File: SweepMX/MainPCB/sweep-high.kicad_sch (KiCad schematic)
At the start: 54 parts, among them J1 AudioJack4dpb, J2 AudioJack4dpb, SW10 SW_Push, SW10_r1 SW_Push, SW11 SW_Push, SW11_r1 SW_Push, SW12 SW_Push, SW12_r1 SW_Push, SW13_r1 SW_Push, SW14 SW_Push, SW14_r1 SW_Push, SW15 SW_Push, SW15_r1 SW_Push, SW16 SW_Push, SW16_r1 SW_Push, SW17 SW_Push, SW17_r1 SW_Push, SW18 SW_Push, SW18_r1 SW_Push, SW2 SW_Push, SW20 SW_Push, SW21 SW_Push, SW2_r1 SW_Push, SW3 SW_Push, SW3_r1 SW_Push, SW4 SW_Push, SW4_r1 SW_Push, SW5 SW_Push, SW5_r1 SW_Push, SW6 SW_Push, SW6_r1 SW_Push, SW7_r1 SW_Push, SW8 SW_Push, SW8_r1 SW_Push, SW9 SW_Push, SW9_r1 SW_Push, U1 ProMicro-kbd, U2 ProMicro-kbd

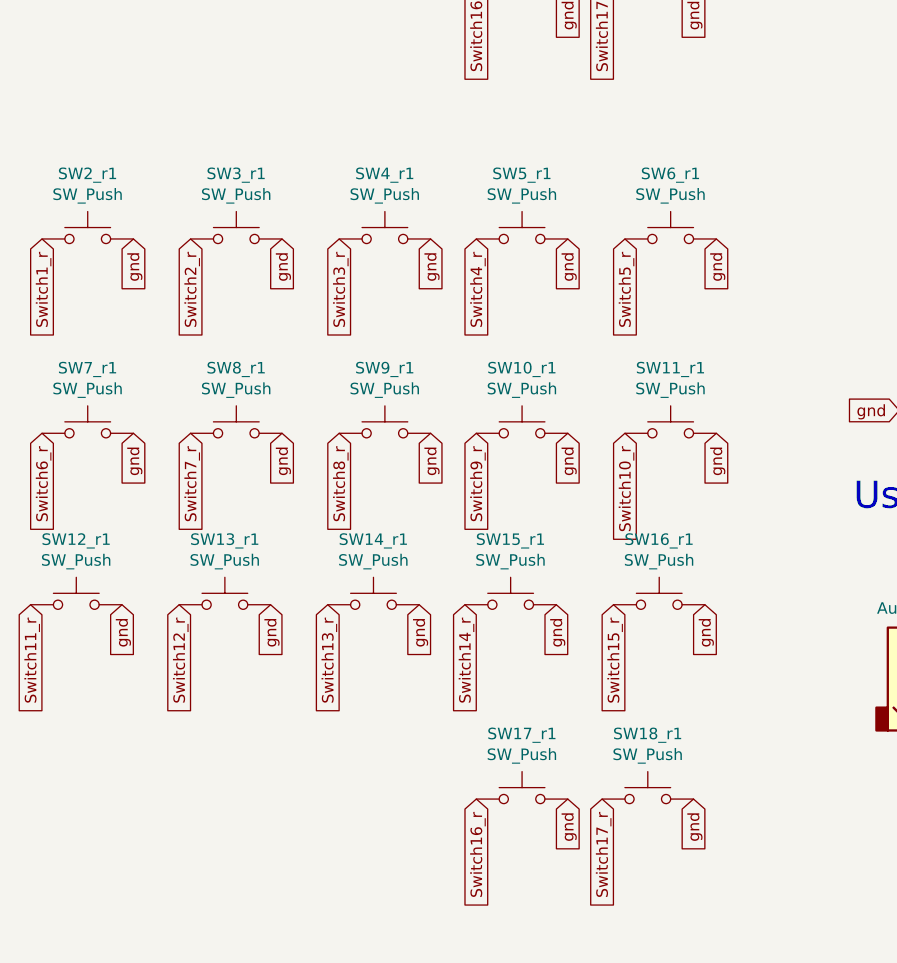
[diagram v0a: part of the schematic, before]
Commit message: sorted schematic and PCB for MX ver
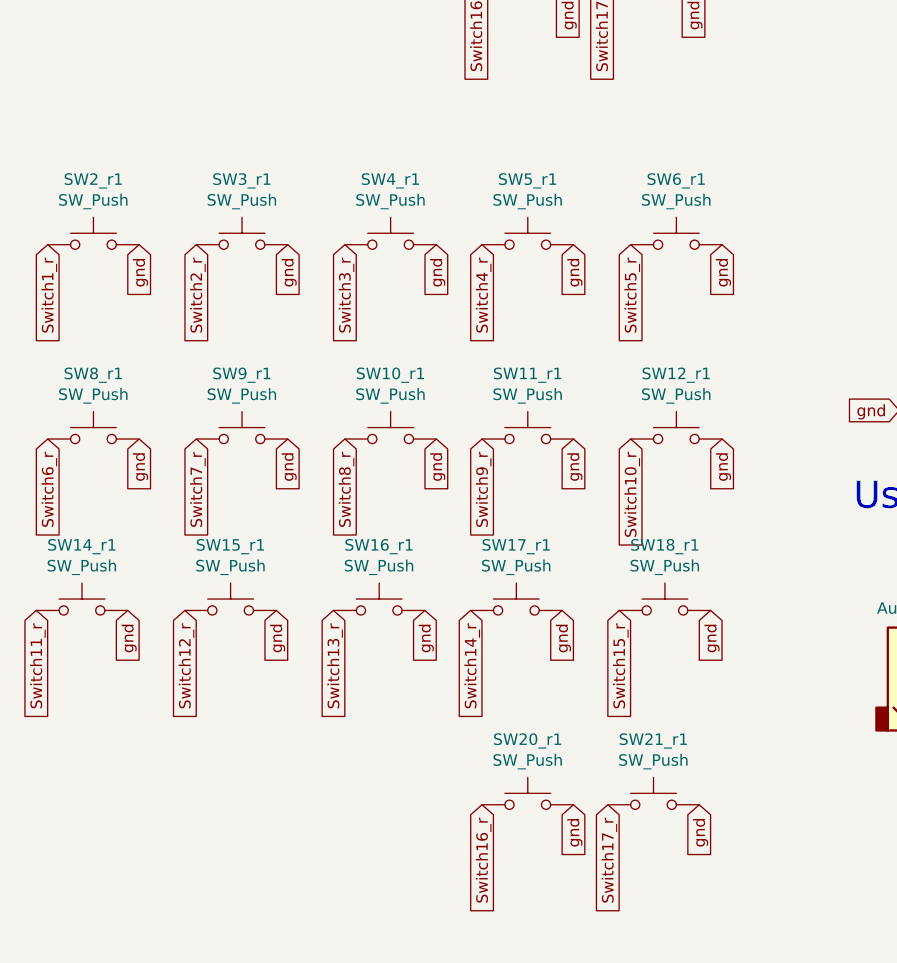
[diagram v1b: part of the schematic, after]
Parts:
- removed SW13_r1, SW7_r1: SW_Push, kbd:CherryMX_Choc_1u, symbol Switch:SW_Push
- added SW20_r1, SW21_r1: SW_Push, kbd:CherryMX_Choc_1u, symbol Switch:SW_Push
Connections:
- net Switch10_r: now also SW12_r1.1; no longer SW11_r1.1
- net Switch11_r: now also SW14_r1.1; no longer SW12_r1.1
- net Switch12_r: now also SW15_r1.1
- net Switch13_r: now also SW16_r1.1; no longer SW14_r1.1
- net Switch14_r: now also SW17_r1.1; no longer SW15_r1.1
- net Switch15_r: now also SW18_r1.1; no longer SW16_r1.1
- net Switch16_r: now also SW20_r1.1; no longer SW17_r1.1
- net Switch17_r: now also SW21_r1.1; no longer SW18_r1.1
- net Switch6_r: now also SW8_r1.1
- net Switch7_r: now also SW9_r1.1; no longer SW8_r1.1
- net Switch8_r: now also SW10_r1.1; no longer SW9_r1.1
- net Switch9_r: now also SW11_r1.1; no longer SW10_r1.1
- net gnd: now also SW20_r1.2, SW21_r1.2
